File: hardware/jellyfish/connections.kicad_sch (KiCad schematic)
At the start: 21 parts, among them J1 INS, J10 Stemma QT, J2 8P8C_LED_Shielded, J3 CAM, J4 CAMLED, J5 OUT1, J6 BLTOUCH, U5 74HC2G34, U6 TVS, U7 74HC2G34

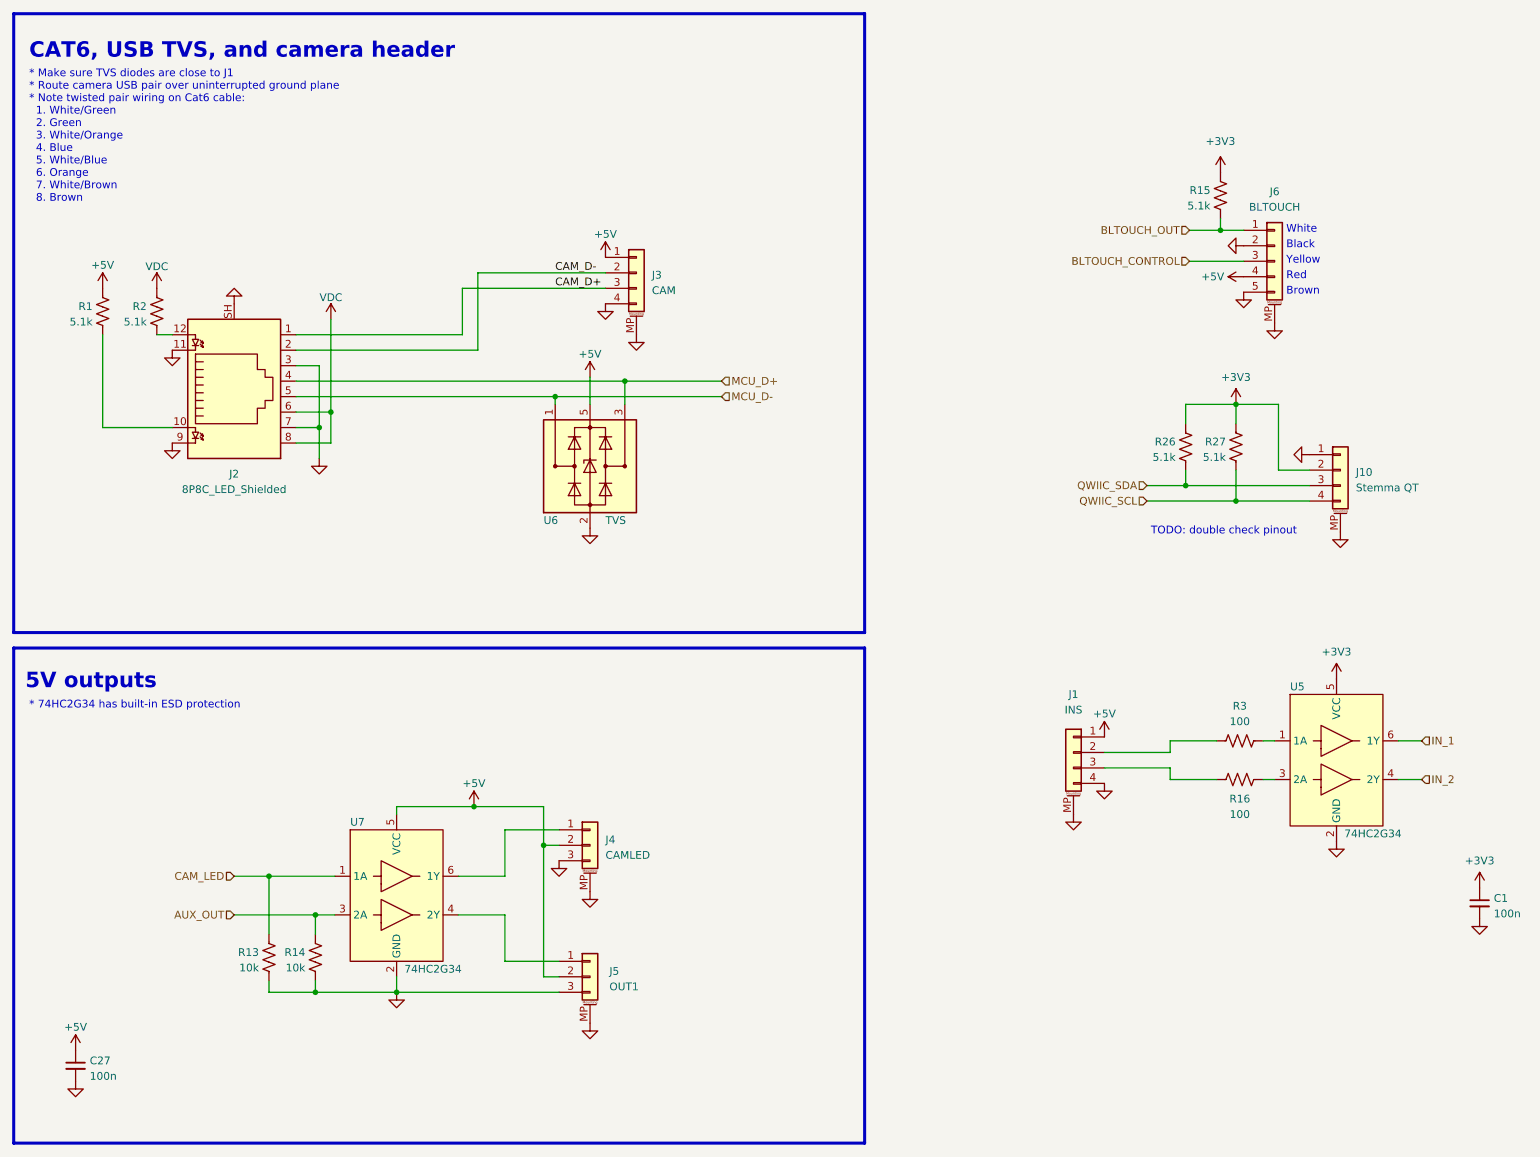
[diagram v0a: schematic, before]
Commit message: Update Jellyfish with some stuff from Starfish
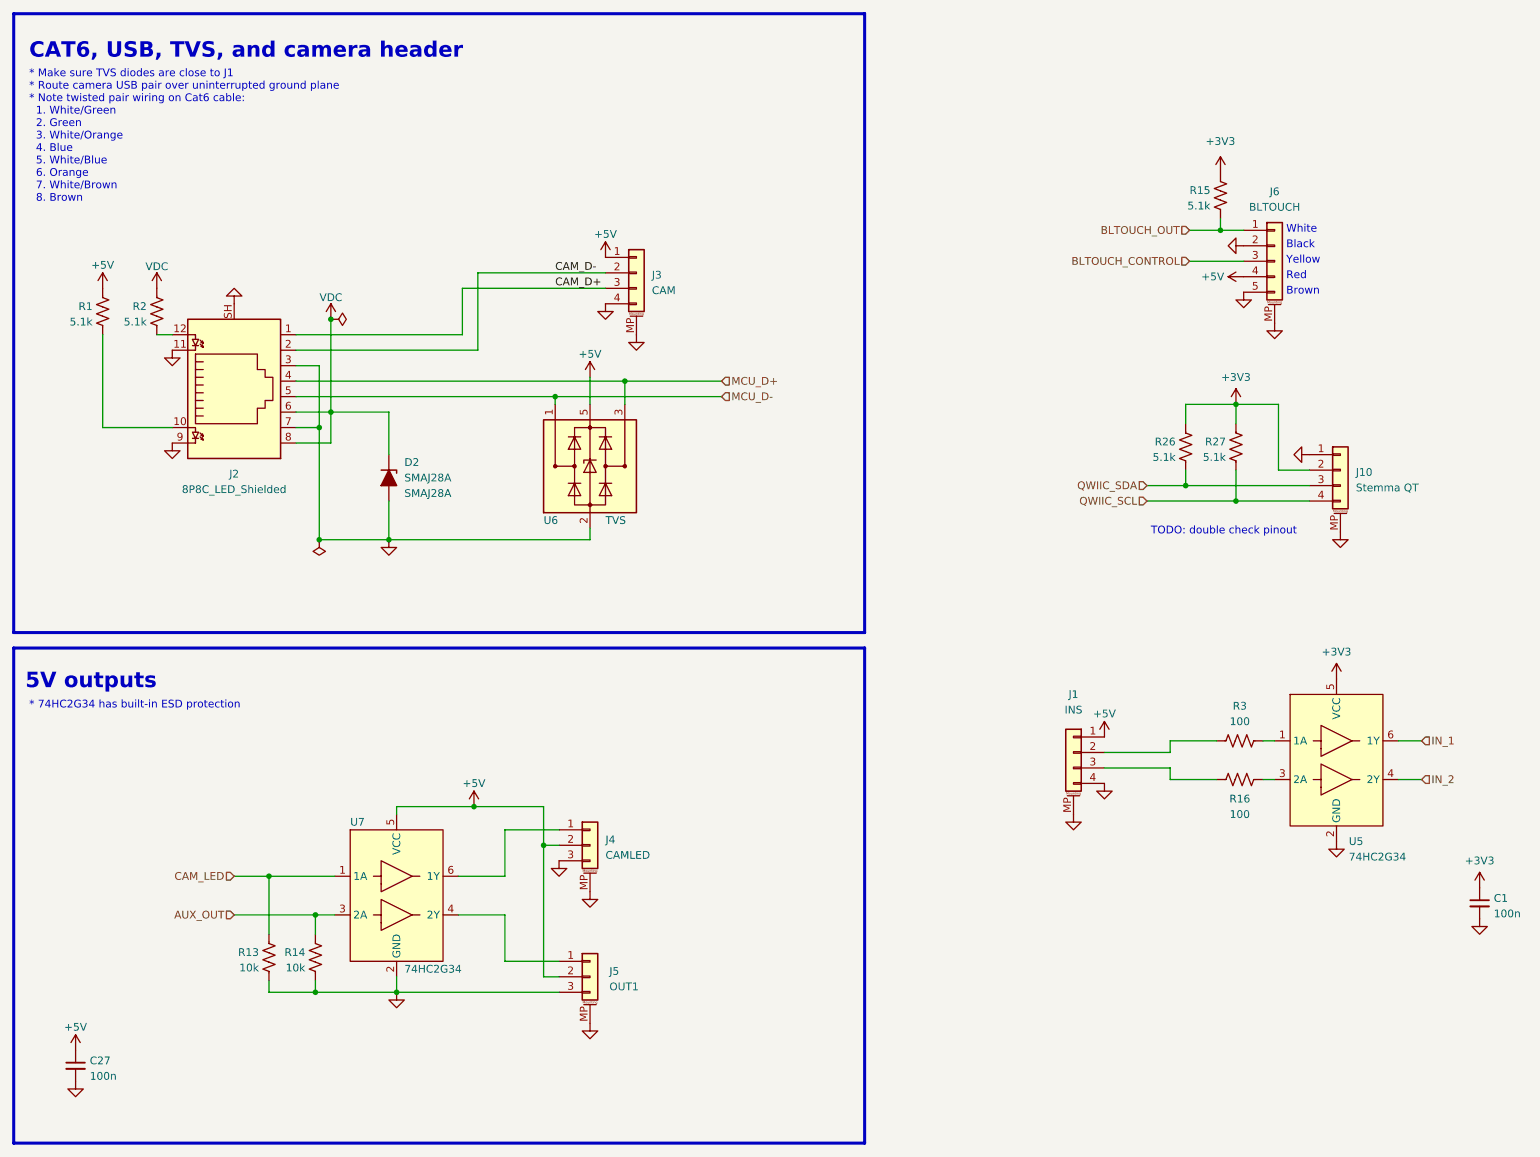
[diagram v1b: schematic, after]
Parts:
- added D2: SMAJ28A, winterbloom:D_SMA, symbol Device:D_Zener_Filled
- C1, C27: footprint Capacitor_SMD:C_0402_1005Metric_Pad0.74x0.62mm_HandSolder -> winterbloom:C_0402_HandSolder
- J1, J10, J3: footprint Connector_JST:JST_SH_SM04B-SRSS-TB_1x04-1MP_P1.00mm_Horizontal -> winterbloom:JST_SH_SM04B-SRSS-TB_1x04-1MP_P1.00mm_Horizontal
- R1, R13, R14, R15, R16, R2, R26, R27, R3: footprint Resistor_SMD:R_0402_1005Metric_Pad0.72x0.64mm_HandSolder -> winterbloom:R_0402_HandSolder
- U5, U7: MPN (none) -> 74HC2G34GW,125
- U6: MPN (none) -> SRL05-TP
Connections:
- net GND: now also D2.2 (A)
- net VDC: now also D2.1 (K)
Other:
- note added: "CAT6, USB, TVS, and camera header"
- note removed: "CAT6, USB TVS, and camera header"
